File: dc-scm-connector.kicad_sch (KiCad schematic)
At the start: 1 part, among them J1 PCB-Edge_DC-SCM-2.1_2x84_Rev-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

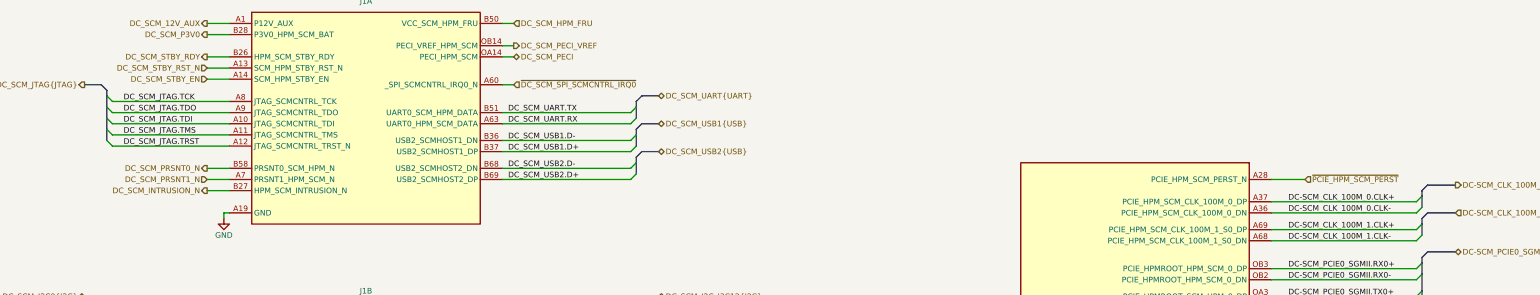
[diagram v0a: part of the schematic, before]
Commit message: [#82323] Connect OSM signals
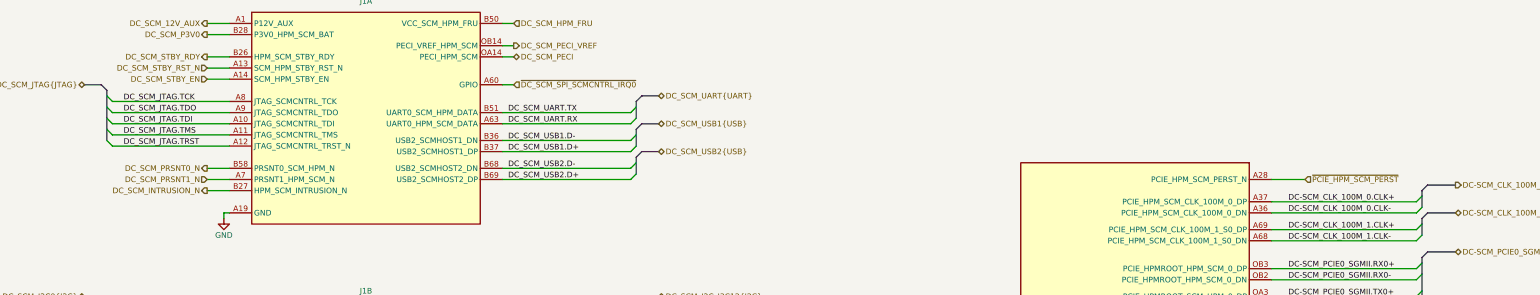
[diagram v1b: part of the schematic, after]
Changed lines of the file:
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@@
 	)
 	(hierarchical_label "DC_SCM_JTAG{JTAG}"
-		(shape output)
+		(shape bidirectional)
 		(at 40.64 58.42 180)
 		(effects
@@
 	)
 	(hierarchical_label "DC-SCM_CLK_100M_1{PCIeREFCLK}"
-		(shape input)
+		(shape bidirectional)
 		(at 353.06 87.63 0)
 		(effects
@@
 		)
 		(pin "A60"
-			(alternate "_SPI_SCMCNTRL_IRQ0_N")
 		)
 		(pin "OA14"
@@
 		)
 		(pin "A60"
-			(alternate "_SPI_SCMCNTRL_IRQ0_N")
 		)
 		(pin "OA14"
@@
 		)
 		(pin "A60"
-			(alternate "_SPI_SCMCNTRL_IRQ0_N")
 		)
 		(pin "OA14"

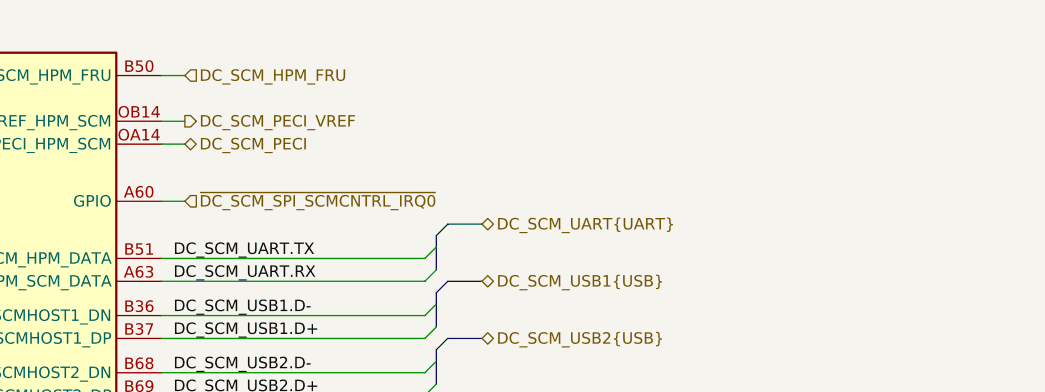
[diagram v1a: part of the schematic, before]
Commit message: [#82323] Add note about PECI voltage translator
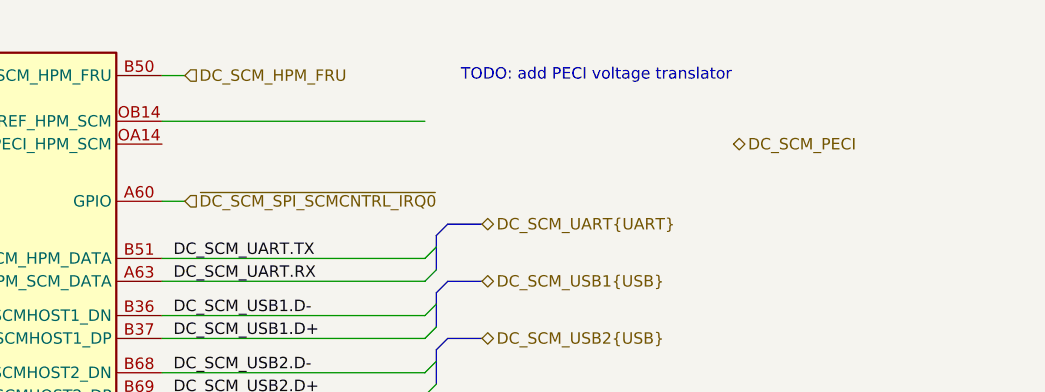
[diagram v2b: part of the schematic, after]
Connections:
- net DC_SCM_PECI: no longer J1.OA14 (PECI_HPM_SCM)
- net DC_SCM_PECI_VREF: no longer names the net of J1.OB14 (PECI_VREF_HPM_SCM)
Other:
- note added: "TODO: add PECI voltage translator"
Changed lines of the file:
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@@
 		(rev "1.0.0")
 	)
+	(text "TODO: add PECI voltage translator"
+		(exclude_from_sim no)
+		(at 184.15 44.45 0)
+		(effects
+			(font
+				(size 1.27 1.27)
+			)
+		)
+	)
 	(no_connect
 		(at 311.15 179.07)
@@
 	(wire
 		(pts
-			(xy 138.43 49.53) (xy 135.89 49.53)
+			(xy 135.89 49.53) (xy 165.1 49.53)
 		)
 		(stroke
@@
 	(wire
 		(pts
-			(xy 138.43 52.07) (xy 135.89 52.07)
-		)
-		(stroke
-			(width 0)
-			(type default)
-		)
-	)
-	(wire
-		(pts
 			(xy 311.15 123.19) (xy 344.17 123.19)
 		)
@@
 	(hierarchical_label "DC_SCM_PECI"
 		(shape bidirectional)
-		(at 138.43 52.07 0)
-		(effects
-			(font
-				(size 1.27 1.27)
-			)
-			(justify left)
-		)
-	)
-	(hierarchical_label "DC_SCM_PECI_VREF"
-		(shape output)
-		(at 138.43 49.53 0)
+		(at 199.39 52.07 0)
 		(effects
 			(font

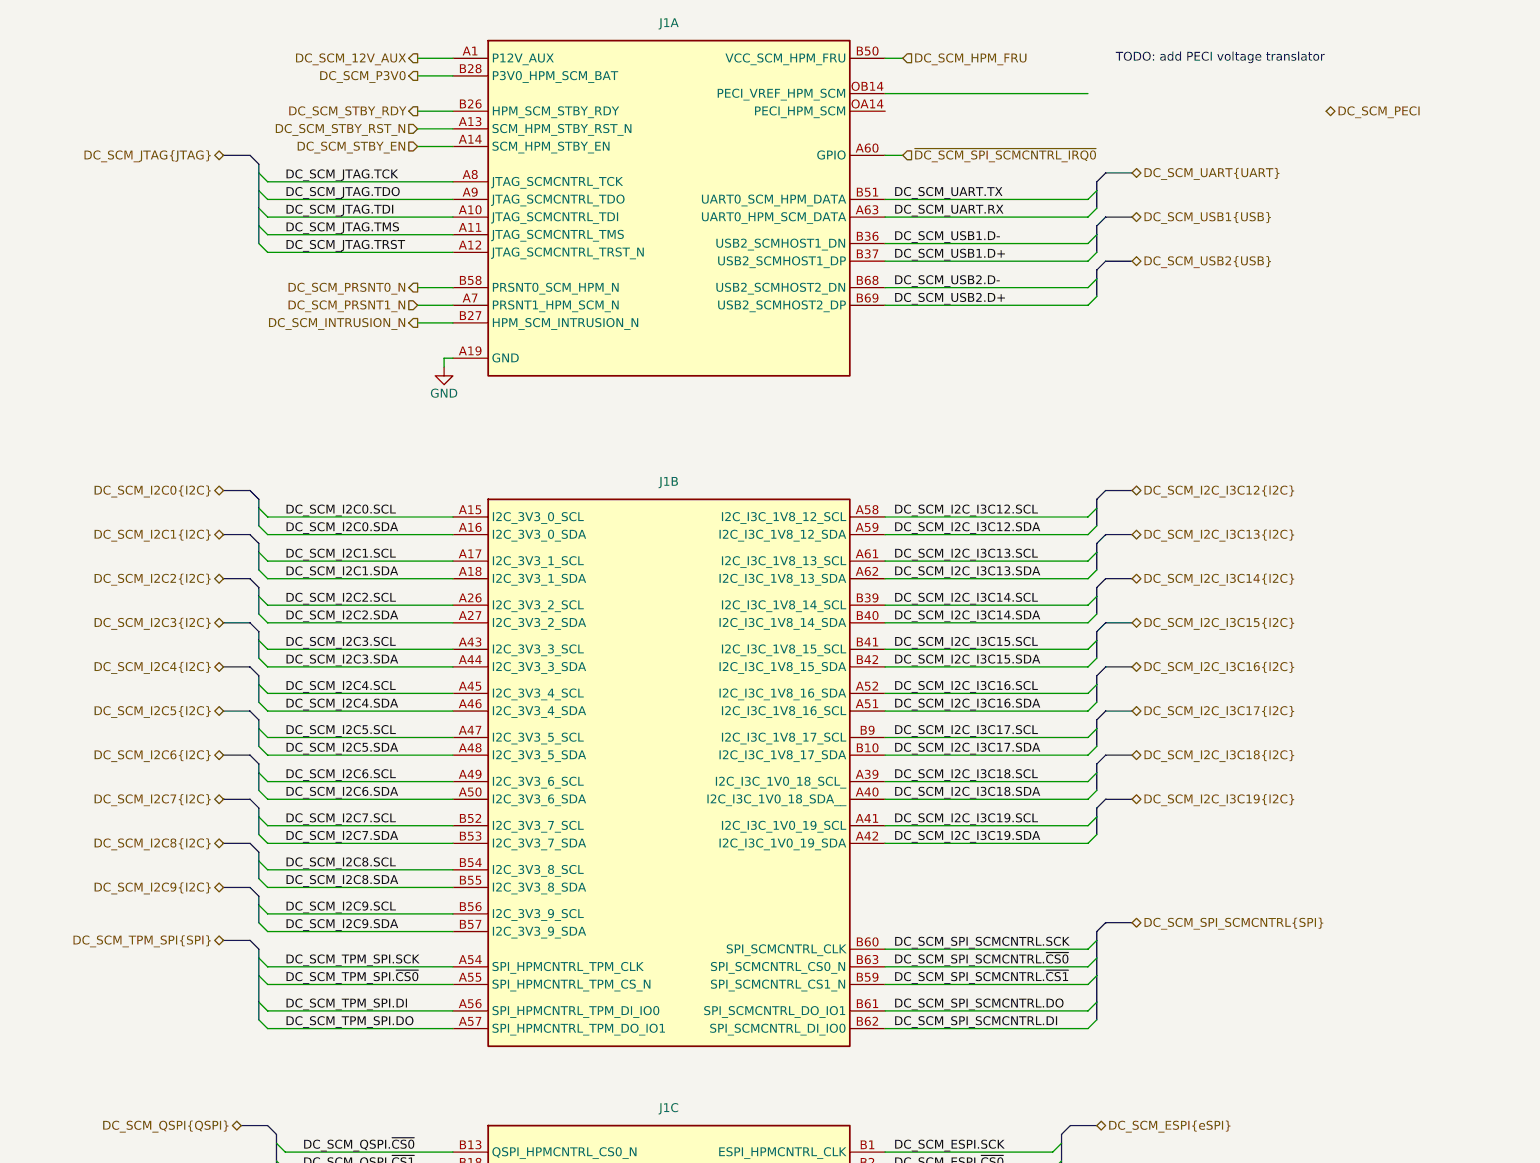
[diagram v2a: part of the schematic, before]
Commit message: [#82688] Add 0R to dc-scm conn
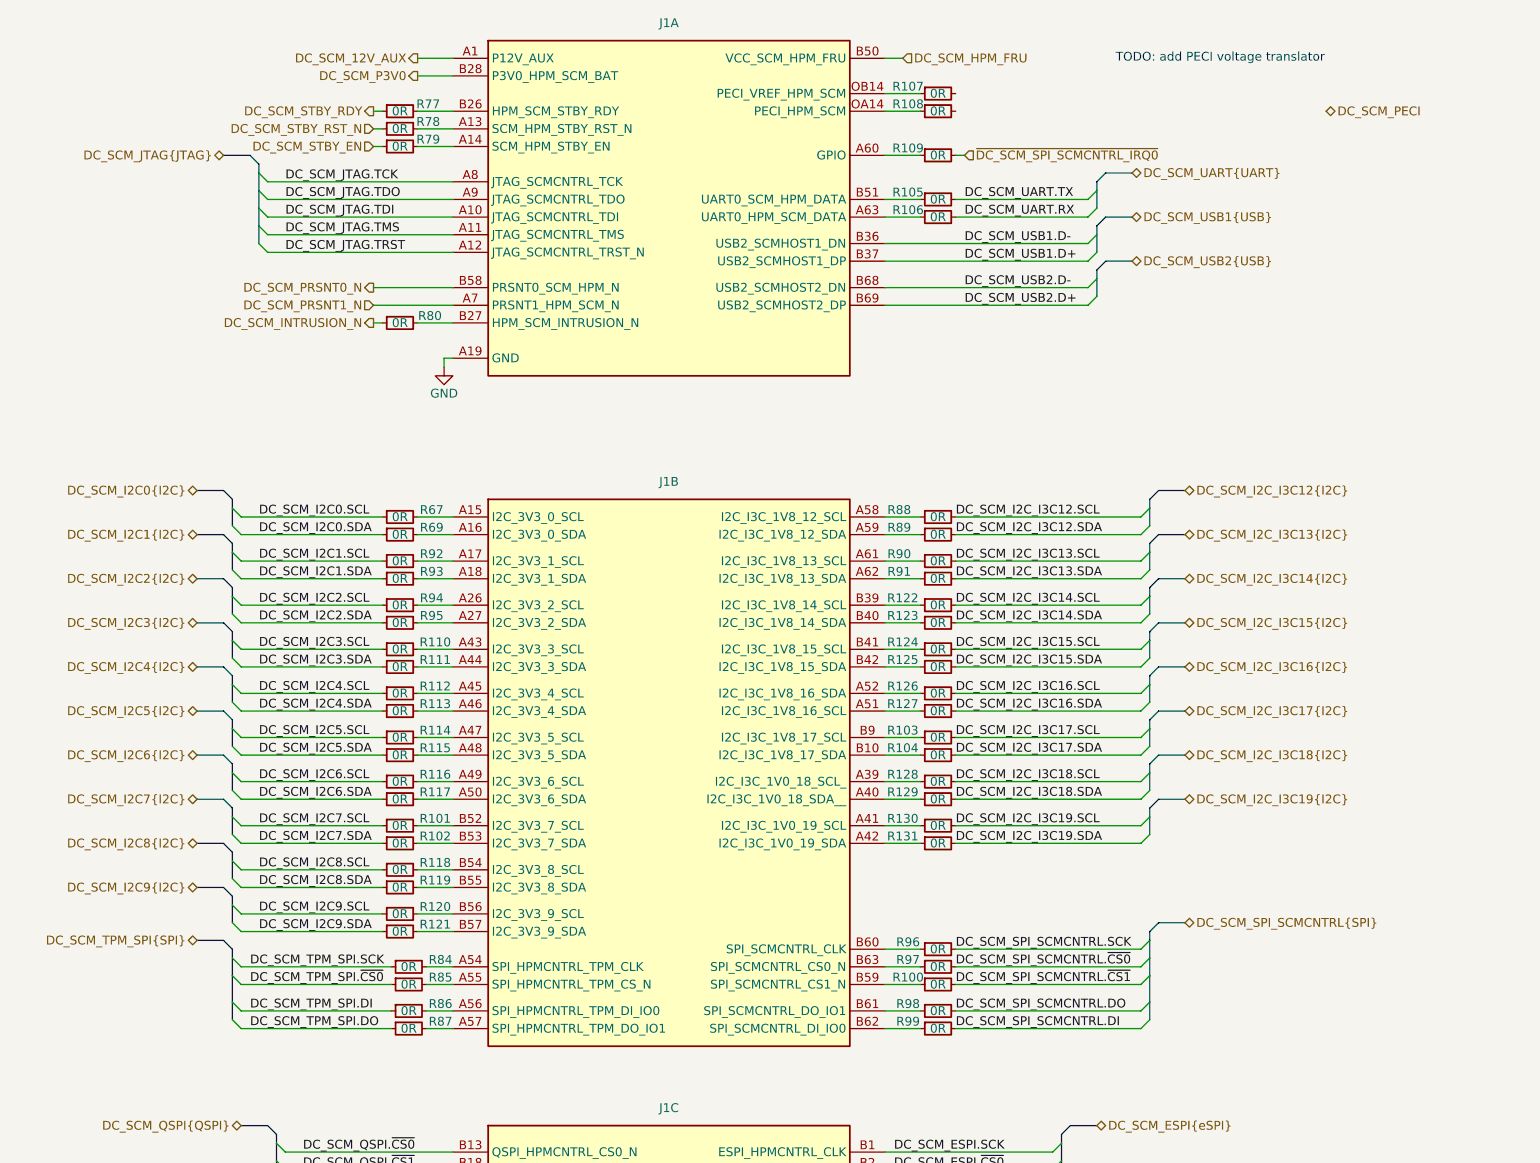
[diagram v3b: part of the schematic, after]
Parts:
- added R100, R101, R102, R103, R104, R105, R106, R107, R108, R109, R110, R111, R112, R113, R114, R115, R116, R117, R118, R119, R120, R121, R122, R123, R124, R125, R126, R127, R128, R129, R130, R131, R67, R69, R77, R78, R79, R80, R84, R85, R86, R87, R88, R89, R90, R91, R92, R93, R94, R95, R96, R97, R98, R99: R_0R_0402, antmicro-footprints:R_0402_1005Metric, symbol antmicroResistors0402:R_0R_0402
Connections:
- net DC_SCM_I2C0.SCL: now also R67.1; no longer J1.A15 (I2C_3V3_0_SCL)
- net DC_SCM_I2C0.SDA: now also R69.1; no longer J1.A16 (I2C_3V3_0_SDA)
- net DC_SCM_I2C1.SCL: now also R92.1; no longer J1.A17 (I2C_3V3_1_SCL)
- net DC_SCM_I2C1.SDA: now also R93.1; no longer J1.A18 (I2C_3V3_1_SDA)
- net DC_SCM_I2C2.SCL: now also R94.1; no longer J1.A26 (I2C_3V3_2_SCL)
- net DC_SCM_I2C2.SDA: now also R95.1; no longer J1.A27 (I2C_3V3_2_SDA)
- net DC_SCM_I2C3.SCL: now also R110.1; no longer J1.A43 (I2C_3V3_3_SCL)
- net DC_SCM_I2C3.SDA: now also R111.1; no longer J1.A44 (I2C_3V3_3_SDA)
- net DC_SCM_I2C4.SCL: now also R112.1; no longer J1.A45 (I2C_3V3_4_SCL)
- net DC_SCM_I2C4.SDA: now also R113.1; no longer J1.A46 (I2C_3V3_4_SDA)
- net DC_SCM_I2C5.SCL: now also R114.1; no longer J1.A47 (I2C_3V3_5_SCL)
- net DC_SCM_I2C5.SDA: now also R115.1; no longer J1.A48 (I2C_3V3_5_SDA)
- net DC_SCM_I2C6.SCL: now also R116.1; no longer J1.A49 (I2C_3V3_6_SCL)
- net DC_SCM_I2C6.SDA: now also R117.1; no longer J1.A50 (I2C_3V3_6_SDA)
- net DC_SCM_I2C7.SCL: now also R101.1; no longer J1.B52 (I2C_3V3_7_SCL)
- net DC_SCM_I2C7.SDA: now also R102.1; no longer J1.B53 (I2C_3V3_7_SDA)
- net DC_SCM_I2C8.SCL: now also R118.1; no longer J1.B54 (I2C_3V3_8_SCL)
- net DC_SCM_I2C8.SDA: now also R119.1; no longer J1.B55 (I2C_3V3_8_SDA)
- net DC_SCM_I2C9.SCL: now also R120.1; no longer J1.B56 (I2C_3V3_9_SCL)
- net DC_SCM_I2C9.SDA: now also R121.1; no longer J1.B57 (I2C_3V3_9_SDA)
- net DC_SCM_I2C_I3C12.SCL: now also R88.2; no longer J1.A58 (I2C_I3C_1V8_12_SCL)
- net DC_SCM_I2C_I3C12.SDA: now also R89.2; no longer J1.A59 (I2C_I3C_1V8_12_SDA)
- net DC_SCM_I2C_I3C13.SCL: now also R90.2; no longer J1.A61 (I2C_I3C_1V8_13_SCL)
- net DC_SCM_I2C_I3C13.SDA: now also R91.2; no longer J1.A62 (I2C_I3C_1V8_13_SDA)
- net DC_SCM_I2C_I3C14.SCL: now also R122.2; no longer J1.B39 (I2C_I3C_1V8_14_SCL)
- net DC_SCM_I2C_I3C14.SDA: now also R123.2; no longer J1.B40 (I2C_I3C_1V8_14_SDA)
- net DC_SCM_I2C_I3C15.SCL: now also R124.2; no longer J1.B41 (I2C_I3C_1V8_15_SCL)
- net DC_SCM_I2C_I3C15.SDA: now also R125.2; no longer J1.B42 (I2C_I3C_1V8_15_SDA)
- net DC_SCM_I2C_I3C16.SCL: now also R126.2; no longer J1.A52 (I2C_I3C_1V8_16_SDA)
- net DC_SCM_I2C_I3C16.SDA: now also R127.2; no longer J1.A51 (I2C_I3C_1V8_16_SCL)
- net DC_SCM_I2C_I3C17.SCL: now also R103.2; no longer J1.B9 (I2C_I3C_1V8_17_SCL)
- net DC_SCM_I2C_I3C17.SDA: now also R104.2; no longer J1.B10 (I2C_I3C_1V8_17_SDA)
- net DC_SCM_I2C_I3C18.SCL: now also R128.2; no longer J1.A39 (I2C_I3C_1V0_18_SCL_)
- net DC_SCM_I2C_I3C18.SDA: now also R129.2; no longer J1.A40 (I2C_I3C_1V0_18_SDA__)
- net DC_SCM_I2C_I3C19.SCL: now also R130.2; no longer J1.A41 (I2C_I3C_1V0_19_SCL)
- net DC_SCM_I2C_I3C19.SDA: now also R131.2; no longer J1.A42 (I2C_I3C_1V0_19_SDA)
- net DC_SCM_INTRUSION_N: now also R80.1; no longer J1.B27 (HPM_SCM_INTRUSION_N)
- net DC_SCM_SPI_SCMCNTRL.DI: now also R99.2; no longer J1.B62 (SPI_SCMCNTRL_DI_IO0)
- net DC_SCM_SPI_SCMCNTRL.DO: now also R98.2; no longer J1.B61 (SPI_SCMCNTRL_DO_IO1)
- net DC_SCM_SPI_SCMCNTRL.SCK: now also R96.2; no longer J1.B60 (SPI_SCMCNTRL_CLK)
- net DC_SCM_SPI_SCMCNTRL.~{CS0}: now also R97.2; no longer J1.B63 (SPI_SCMCNTRL_CS0_N)
- net DC_SCM_SPI_SCMCNTRL.~{CS1}: now also R100.2; no longer J1.B59 (SPI_SCMCNTRL_CS1_N)
- net DC_SCM_STBY_EN: now also R79.1; no longer J1.A14 (SCM_HPM_STBY_EN)
- net DC_SCM_STBY_RDY: now also R77.1; no longer J1.B26 (HPM_SCM_STBY_RDY)
- net DC_SCM_STBY_RST_N: now also R78.1; no longer J1.A13 (SCM_HPM_STBY_RST_N)
- net DC_SCM_TPM_SPI.DI: now also R86.1; no longer J1.A56 (SPI_HPMCNTRL_TPM_DI_IO0)
- net DC_SCM_TPM_SPI.DO: now also R87.1; no longer J1.A57 (SPI_HPMCNTRL_TPM_DO_IO1)
- net DC_SCM_TPM_SPI.SCK: now also R84.1; no longer J1.A54 (SPI_HPMCNTRL_TPM_CLK)
- net DC_SCM_TPM_SPI.~{CS0}: now also R85.1; no longer J1.A55 (SPI_HPMCNTRL_TPM_CS_N)
- net DC_SCM_UART.RX: now also R106.2; no longer J1.A63 (UART0_HPM_SCM_DATA)
- net DC_SCM_UART.TX: now also R105.2; no longer J1.B51 (UART0_SCM_HPM_DATA)
- net ~{DC_SCM_SPI_SCMCNTRL_IRQ0}: now also R109.2; no longer J1.A60 (GPIO)
- net at J1.OA14 (PECI_HPM_SCM): now also R108.1
- net at J1.OB14 (PECI_VREF_HPM_SCM): now also R107.1
- new net: J1.A27 (I2C_3V3_2_SDA), R95.2
- new net: J1.A40 (I2C_I3C_1V0_18_SDA__), R129.1
- new net: J1.A60 (GPIO), R109.1
- new net: J1.B40 (I2C_I3C_1V8_14_SDA), R123.1
- new net: J1.B42 (I2C_I3C_1V8_15_SDA), R125.1
- new net: J1.A15 (I2C_3V3_0_SCL), R67.2
- new net: J1.A17 (I2C_3V3_1_SCL), R92.2
- new net: J1.A42 (I2C_I3C_1V0_19_SDA), R131.1
- new net: J1.B61 (SPI_SCMCNTRL_DO_IO1), R98.1
- new net: J1.B26 (HPM_SCM_STBY_RDY), R77.2
- new net: J1.A13 (SCM_HPM_STBY_RST_N), R78.2
- new net: J1.A47 (I2C_3V3_5_SCL), R114.2
- new net: J1.A45 (I2C_3V3_4_SCL), R112.2
- new net: J1.B59 (SPI_SCMCNTRL_CS1_N), R100.1
- new net: J1.A61 (I2C_I3C_1V8_13_SCL), R90.1
- new net: J1.B52 (I2C_3V3_7_SCL), R101.2
- new net: J1.B54 (I2C_3V3_8_SCL), R118.2
- new net: J1.A14 (SCM_HPM_STBY_EN), R79.2
- new net: J1.B53 (I2C_3V3_7_SDA), R102.2
- new net: J1.B39 (I2C_I3C_1V8_14_SCL), R122.1
- new net: J1.A51 (I2C_I3C_1V8_16_SCL), R127.1
- new net: J1.A63 (UART0_HPM_SCM_DATA), R106.1
- new net: J1.B27 (HPM_SCM_INTRUSION_N), R80.2
- new net: J1.B51 (UART0_SCM_HPM_DATA), R105.1
- new net: J1.B60 (SPI_SCMCNTRL_CLK), R96.1
- new net: J1.A16 (I2C_3V3_0_SDA), R69.2
- new net: J1.B63 (SPI_SCMCNTRL_CS0_N), R97.1
- new net: J1.A56 (SPI_HPMCNTRL_TPM_DI_IO0), R86.2
- new net: J1.B41 (I2C_I3C_1V8_15_SCL), R124.1
- new net: J1.B55 (I2C_3V3_8_SDA), R119.2
- new net: J1.A49 (I2C_3V3_6_SCL), R116.2
- new net: J1.A41 (I2C_I3C_1V0_19_SCL), R130.1
- new net: J1.B10 (I2C_I3C_1V8_17_SDA), R104.1
- new net: J1.B56 (I2C_3V3_9_SCL), R120.2
- new net: J1.A55 (SPI_HPMCNTRL_TPM_CS_N), R85.2
- new net: J1.B9 (I2C_I3C_1V8_17_SCL), R103.1
- new net: J1.A62 (I2C_I3C_1V8_13_SDA), R91.1
- new net: J1.B57 (I2C_3V3_9_SDA), R121.2
- new net: J1.A39 (I2C_I3C_1V0_18_SCL_), R128.1
- new net: J1.A46 (I2C_3V3_4_SDA), R113.2
- new net: J1.A57 (SPI_HPMCNTRL_TPM_DO_IO1), R87.2
- new net: J1.A50 (I2C_3V3_6_SDA), R117.2
- new net: J1.A59 (I2C_I3C_1V8_12_SDA), R89.1
- new net: J1.A18 (I2C_3V3_1_SDA), R93.2
- new net: J1.A26 (I2C_3V3_2_SCL), R94.2
- new net: J1.A43 (I2C_3V3_3_SCL), R110.2
- new net: J1.A44 (I2C_3V3_3_SDA), R111.2
- new net: J1.A48 (I2C_3V3_5_SDA), R115.2
- new net: J1.A52 (I2C_I3C_1V8_16_SDA), R126.1
- new net: J1.A54 (SPI_HPMCNTRL_TPM_CLK), R84.2
- new net: J1.A58 (I2C_I3C_1V8_12_SCL), R88.1
- new net: J1.B62 (SPI_SCMCNTRL_DI_IO0), R99.1
